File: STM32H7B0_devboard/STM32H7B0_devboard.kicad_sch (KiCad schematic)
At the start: 56 parts, among them J1 SWD, J2 24LC512 socet, Q2 S8050, SW1 BOOT_SEL, U1 STM32H7B0VBT6, Y1 25MHz, Y2 32.768KHz

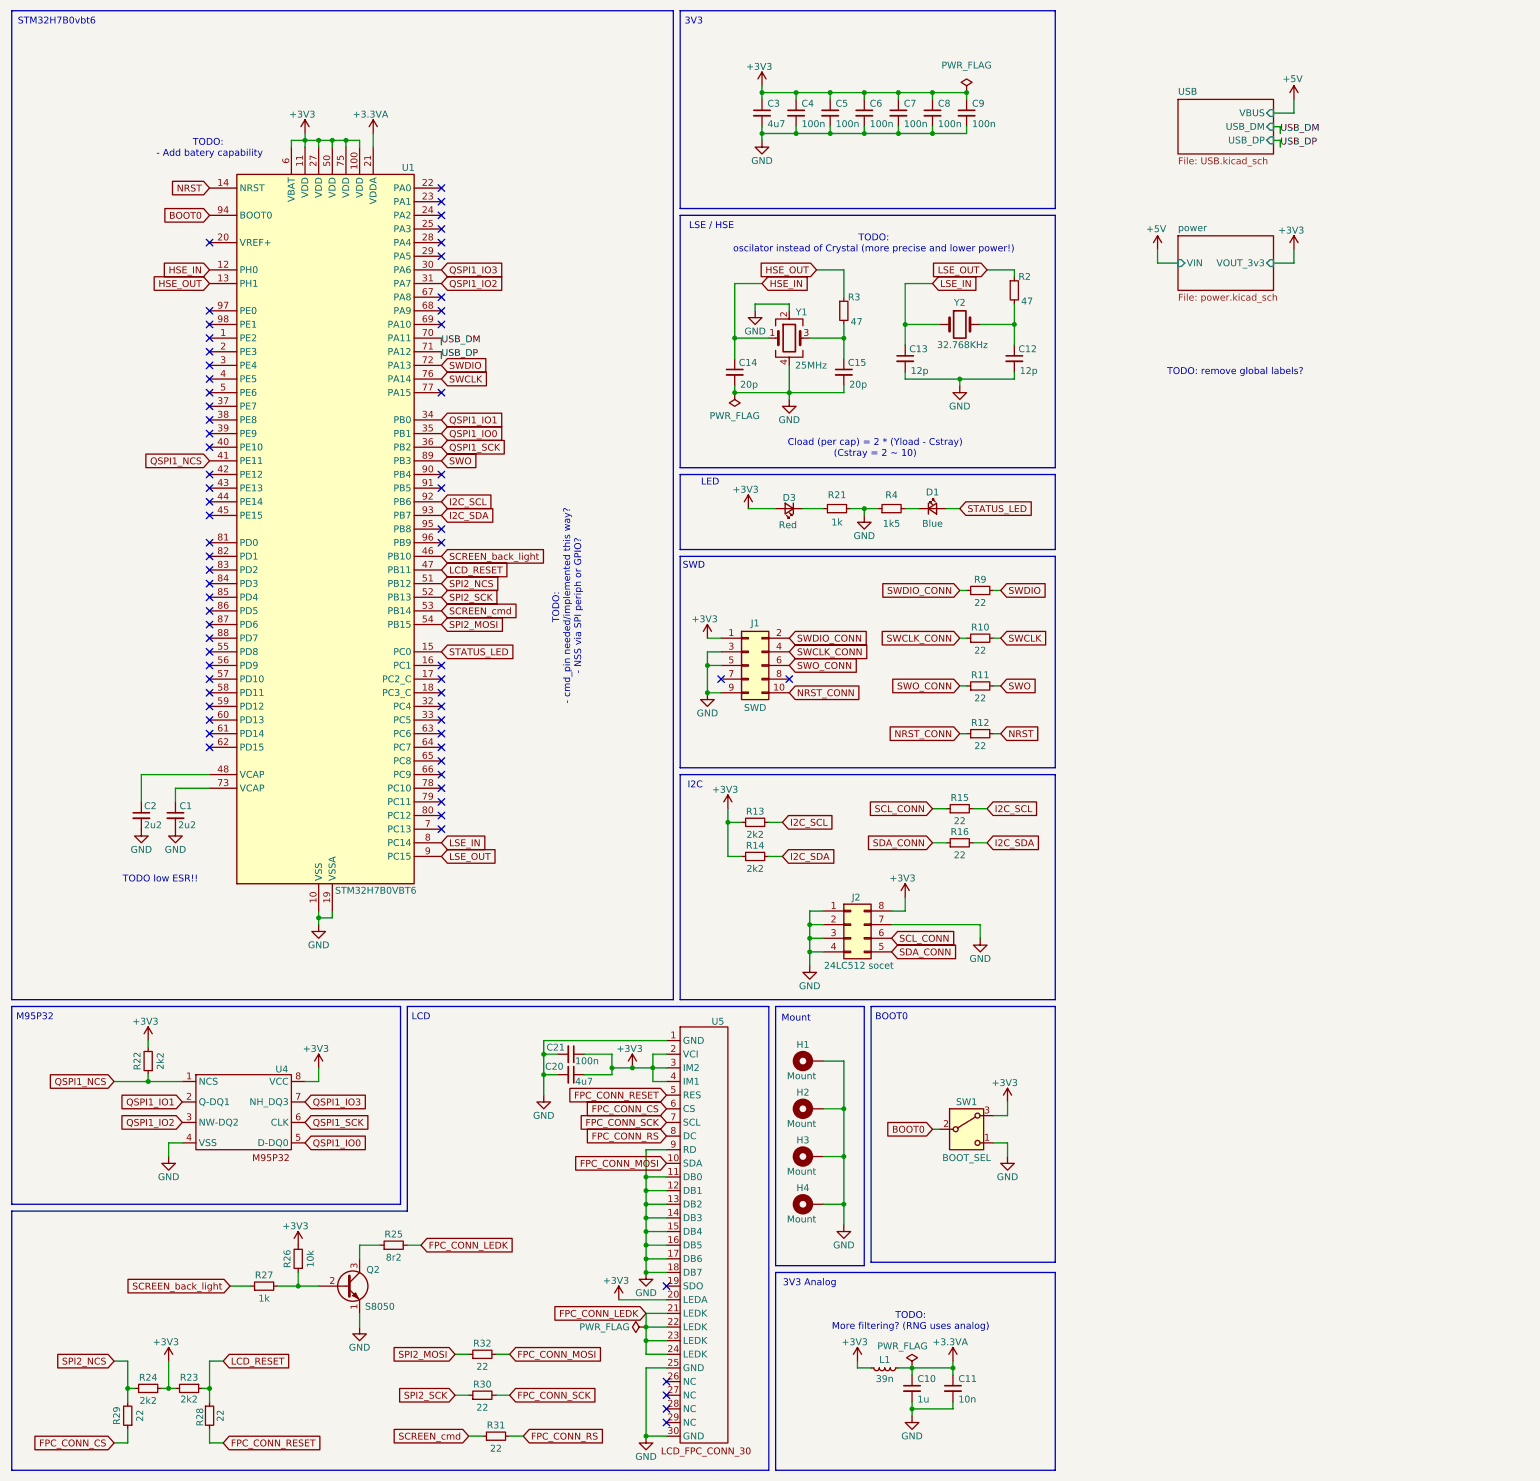
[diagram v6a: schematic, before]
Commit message: Sorted schematic components
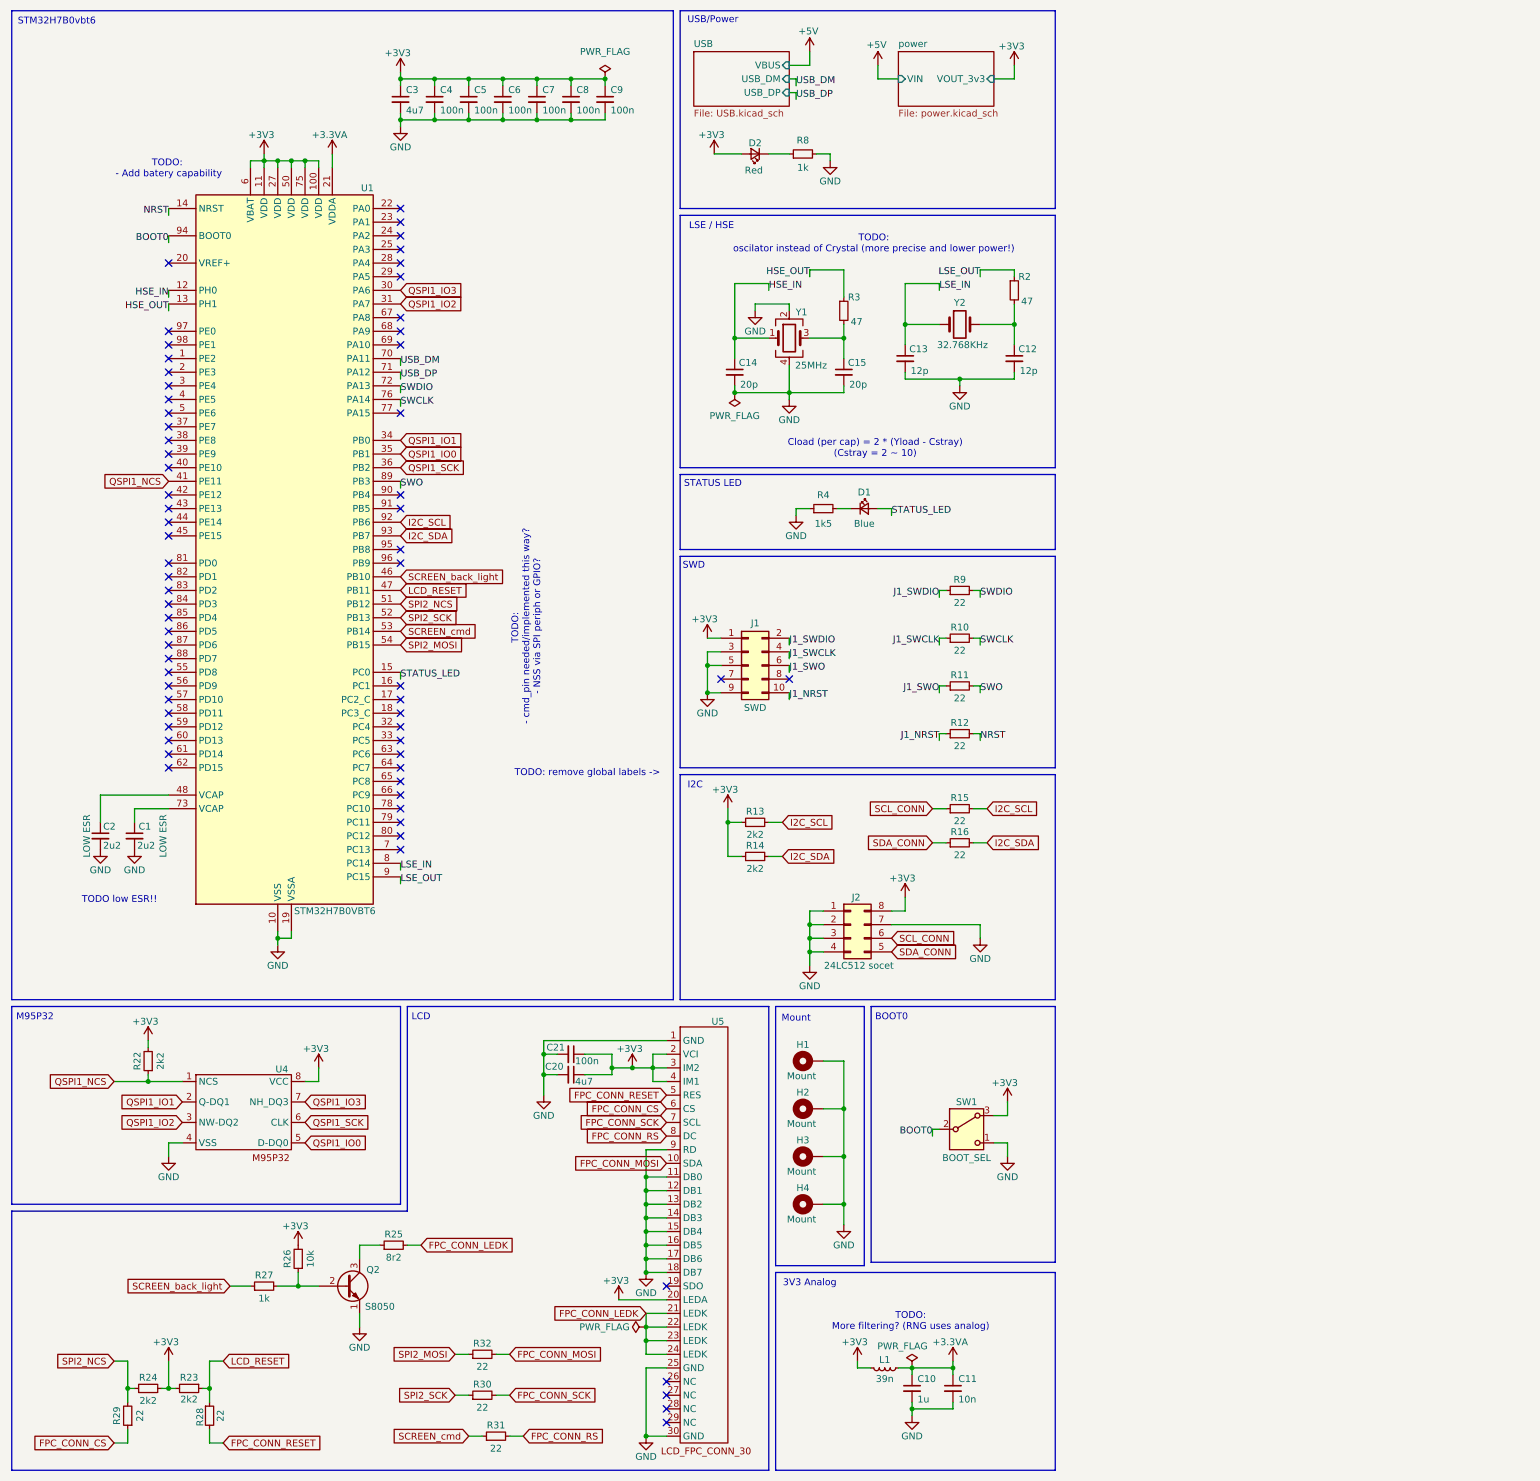
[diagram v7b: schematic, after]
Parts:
- removed D3: Red, Diode_SMD:D_0603_1608Metric, symbol Device:LED_Small
- removed R21: 1k, symbol Device:R_Small
- added D2: Red, Diode_SMD:D_0603_1608Metric, symbol Device:LED_Small
- added R8: 1k, symbol Device:R_Small
- C1, C2: footprint Capacitor_SMD:C_0402_1005Metric -> (none)
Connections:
- net +3V3: now also D2.2 (A)
- net GND: now also R8.2
- net NRST_CONN renamed J1_NRST
- net SWCLK_CONN renamed J1_SWCLK
- net SWDIO_CONN renamed J1_SWDIO
- net SWO_CONN renamed J1_SWO
- new net: D2.1 (K), R8.1
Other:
- note added: "STATUS LED"
- note added: "TODO: remove global labels ->"
- note added: "USB/Power"
- note removed: "3V3"
- note removed: "LED"
- note removed: "TODO: remove global labels?"
- moved on the sheet: C1, C2, C3, C4, C5, C6, C7, C8, C9, D1, R10, R11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

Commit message: Schematic done!
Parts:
- removed R15, R16, R30, R31, R32: 22, symbol Device:R_Small
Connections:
- net FPC_CONN_MOSI is gone; now on net SPI2_MOSI: U5.10 (SDA)
- net FPC_CONN_SCK is gone; now on net SPI2_SCK: U5.7 (SCL)
- net SCL_CONN is gone; now on net I2C_SCL: J2.6 (Pin_6)
- net SCREEN_cmd is gone; now on net LCD_COMMAND: U1.53 (PB14)
- net SDA_CONN is gone; now on net I2C_SDA: J2.5 (Pin_5)
- net FPC_CONN_CS renamed LCD_NSS
- net FPC_CONN_LEDK renamed LCD_LEDK
- net FPC_CONN_RESET renamed LCD_RST
- net FPC_CONN_RS renamed LCD_COMMAND
- net QSPI1_NCS renamed QSPI1_NSS
- net SCREEN_back_light renamed LCD_BACKLIGHT
- net SPI2_NCS renamed SPI2_NSS
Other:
- moved on the sheet: C10, C11, C20, C21, H1, H2, H3, H4, J2, L1, SW1, U5
